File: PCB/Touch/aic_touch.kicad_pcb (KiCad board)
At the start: 2 copper layers, 50 x 50 mm, 14 parts, among them J1 Antenna, J2 PN5180, J3 PN532, J4 Display, U1 Pico

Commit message: Fix PCB issue and change to 4020 RGB
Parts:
- D1, D2, D3, D4, D5, D6: footprint aic_pico:WS2812B-1204 -> aic_pico:WS2812B-4020
- moved D1 36.8 mm to (153.7, 122.3)
- moved D2 36.8 mm to (153.7, 104.5)
- moved D5 36.8 mm to (116.9, 104.5)
- moved D6 36.8 mm to (116.9, 122.3)
- moved R1 36.2 mm to (153.1, 126.4)
- moved D3 16.5 mm to (143.6, 95.0), turned to 0 degrees
- moved D4 16.5 mm to (127.1, 95.0), turned to 0 degrees
- moved R2 6.41 mm to (137.1, 102.0), turned to 0 degrees
- moved R3 5.38 mm to (133.5, 102.0)
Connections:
- U1 pad 10: /TP_SCL -> /RST
- U1 pad 11: /TP_RST -> /D/C
- U1 pad 12: /TP_INT -> /CS
- U1 pad 14: unconnected-(U1-GPIO10-Pad14) -> /SCK
- U1 pad 15: unconnected-(U1-GPIO11-Pad15) -> /SDA
- U1 pad 2: /D/C -> unconnected-(U1-GPIO1-Pad2)
- U1 pad 4: /SCK -> /TP_SDA
- U1 pad 5: /SDA -> /TP_SCL
- U1 pad 6: /RST -> /TP_INT
- U1 pad 7: /CS -> /TP_RST
- U1 pad 9: /TP_SDA -> unconnected-(U1-GPIO6-Pad9)
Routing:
- net /RGB: track 31.1 -> 13.4 mm
- net /D/C: track 27.2 -> 12.5 mm
- net +3V3: track 92.4 -> 105.3 mm
- net /SCK: track 23.1 -> 15.9 mm
- net GND: track 204.4 -> 198.1 mm
- net /RST: track 20.5 -> 14.4 mm
- net /TP_SDA: track 18.9 -> 24.8 mm
- net /LEDK: track 32.6 -> 27.3 mm
- net /TP_INT: track 16.3 -> 21.3 mm
- net /TP_RST: track 14.0 -> 19.0 mm
- net Net-(D4-Out): track 16.9 -> 13.3 mm
- net /SDA: track 22.3 -> 18.8 mm
- net +5V: track 153.2 -> 150.3 mm
- net /TP_SCL: track 20.4 -> 22.9 mm
- net Net-(D1-In): track 4.39 -> 1.96 mm
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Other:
- board text added: "AIC Touch v1.1"
- board text removed: "AIC Touch v1.0"

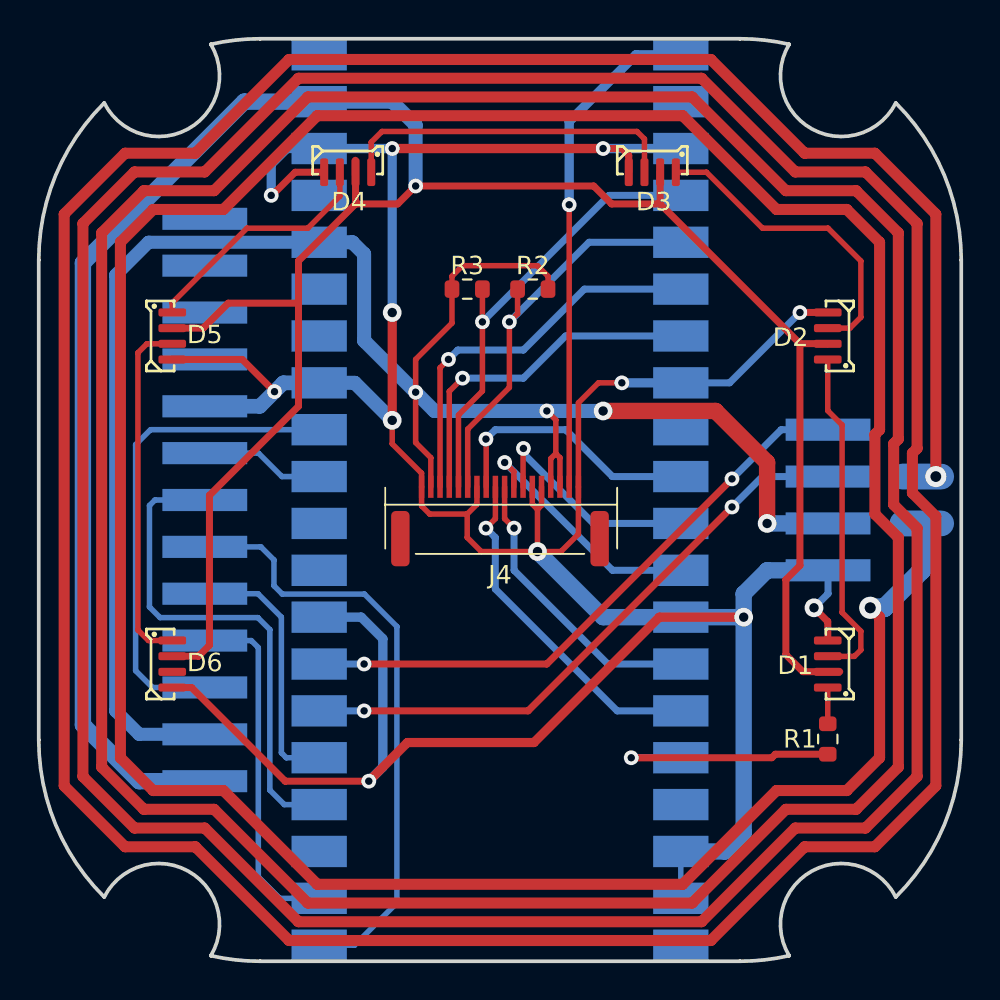
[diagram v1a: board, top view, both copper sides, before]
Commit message: Power filtering for PN5180 on AIC touch
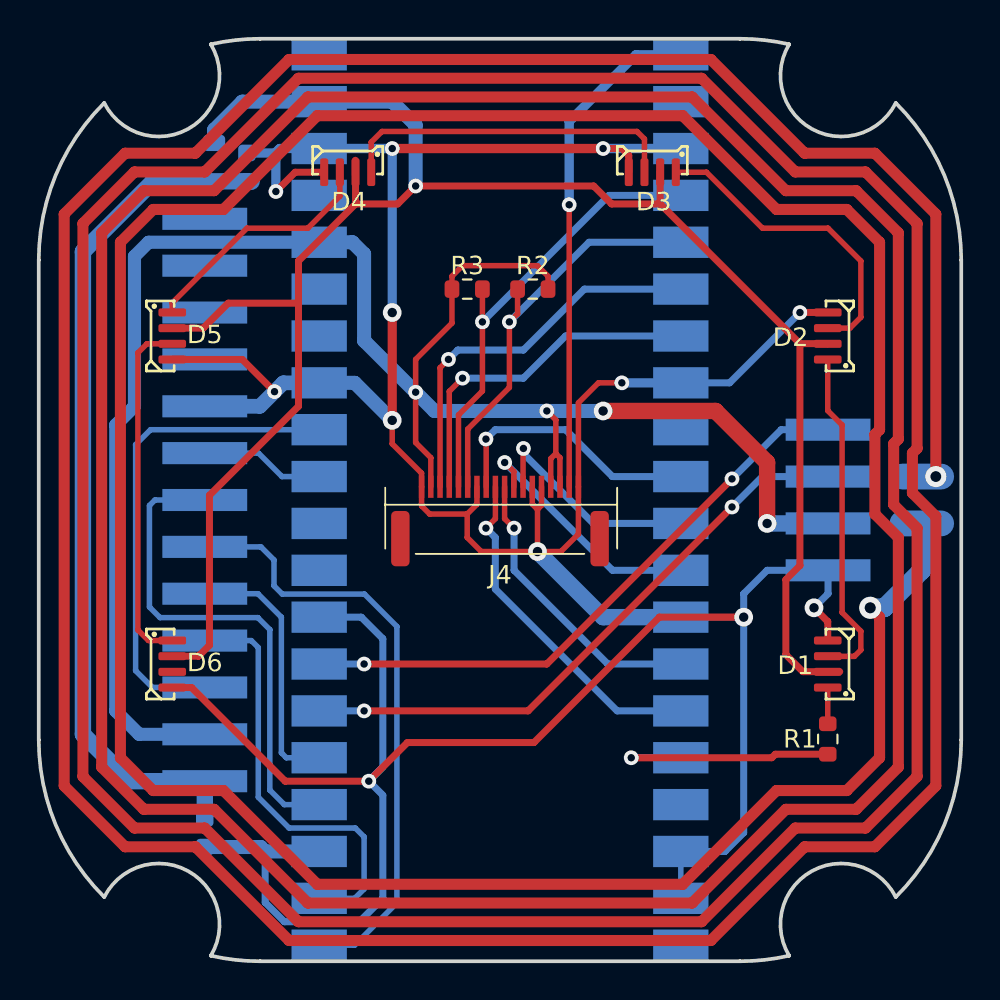
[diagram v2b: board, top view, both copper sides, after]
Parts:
- added C1: 0.1uF, Capacitor_SMD:C_0603_1608Metric, B.Cu at (121.6, 95.4)
- added C2: 10uF, Capacitor_SMD:C_0603_1608Metric, B.Cu at (119.3, 131.4)
- added L1: 100nH, Inductor_SMD:L_0805_2012Metric, B.Cu at (119.8, 95.1)
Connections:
- J2 pad 1: +5V -> Net-(J2-5V)
- U1 pad 23: unconnected-(U1-GND-Pad23) -> GND
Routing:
- net Net-(J2-5V): track 0.00 -> 46.6 mm
- net +5V: track 150.3 -> 107.2 mm
- net GND: track 198.1 -> 222.6 mm
- net Net-(J2-NSS): track 19.3 -> 23.3 mm
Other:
- board text added: "AIC Touch v1.2"
- board text removed: "AIC Touch v1.1"

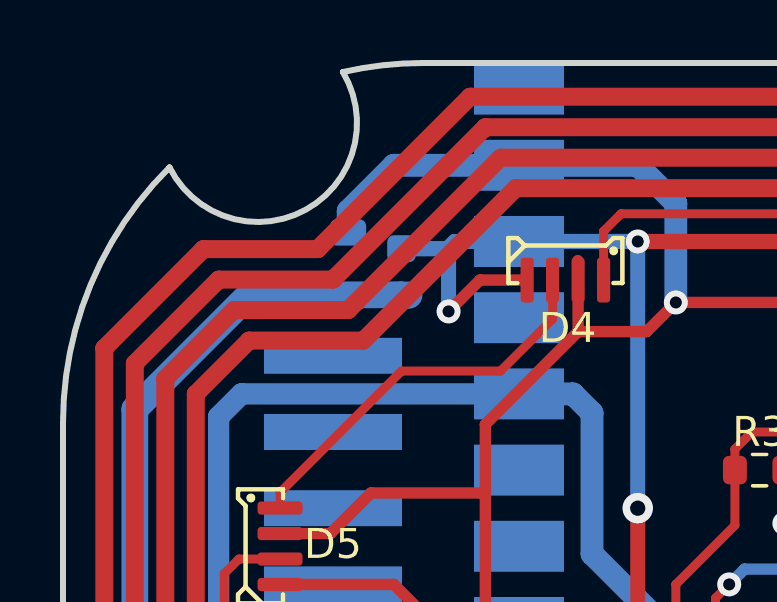
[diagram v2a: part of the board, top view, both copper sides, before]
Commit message: L1 to 1206 and power from VBUS
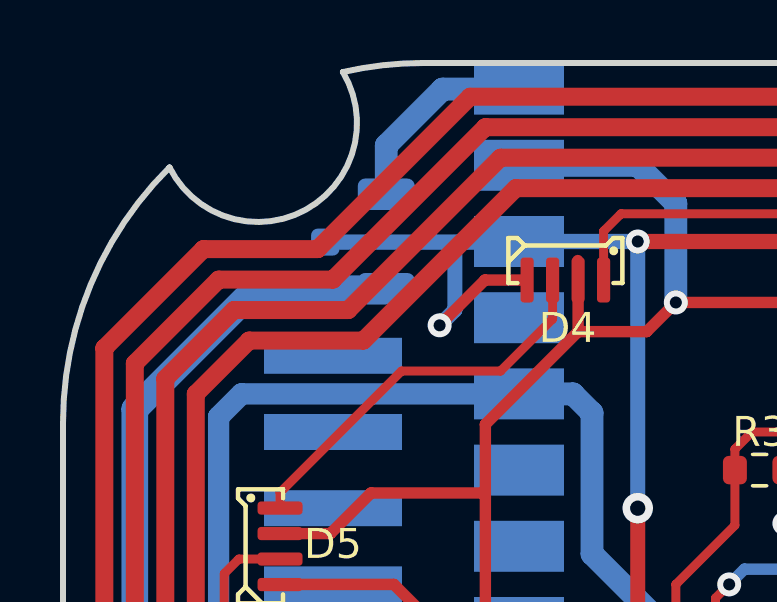
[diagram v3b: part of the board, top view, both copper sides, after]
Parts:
- L1: footprint Inductor_SMD:L_0805_2012Metric -> Inductor_SMD:L_1206_3216Metric
- moved C1 2.55 mm to (119.1, 95.1)
- moved L1 1.48 mm to (121.1, 94.3)
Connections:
- L1 pad 1: +5V -> Net-(U1-VBUS)
- U1 pad 40: unconnected-(U1-VBUS-Pad40) -> Net-(U1-VBUS)
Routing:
- net +5V: track 107.2 -> 100.2 mm
- net Net-(U1-VBUS): track 0.00 -> 6.83 mm
- net GND: track 222.6 -> 226.1 mm
- net Net-(J2-5V): track 46.6 -> 45.9 mm
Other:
- board text added: "AIC Touch v1.21"
- board text removed: "AIC Touch v1.2"

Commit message: Hybrid AIC Key PCB and AIC touch RGB back to 1204
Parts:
- removed L1: 100nH, Inductor_SMD:L_1206_3216Metric
- added C3: 0.1uF, Capacitor_SMD:C_0603_1608Metric, F.Cu at (140.9, 110.1)
- C2: value 10uF -> 0.1uF; moved to F.Cu
- D1, D2, D3, D4, D5, D6: footprint aic_pico:WS2812B-4020 -> aic_pico:WS2812B-1204
- moved R1 35.8 mm to (117.3, 126.6), turned to 0 degrees
- moved D1 35.4 mm to (118.3, 122.4)
- moved D2 35.4 mm to (118.3, 104.4)
- moved D5 35.4 mm to (152.3, 104.4)
- moved D6 35.4 mm to (152.3, 122.4)
- moved C2 24.0 mm to (130.2, 110.1), turned to 180 degrees
- moved D3 17.3 mm to (126.3, 96.4), turned to 180 degrees
- moved D4 17.3 mm to (144.3, 96.4), turned to 180 degrees
- moved C1 2.03 mm to (121.1, 95.1), turned to -90 degrees
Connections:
- C1 pad 1: Net-(J2-5V) -> +5V
- C2 pad 1: Net-(J2-5V) -> +3V3
- J2 pad 1: Net-(J2-5V) -> +5V
- U1 pad 40: Net-(U1-VBUS) -> unconnected-(U1-VBUS-Pad40)
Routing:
- net +5V: track 100.2 -> 146.4 mm
- net Net-(J2-5V): track 45.9 -> 0.00 mm
- net GND: track 226.1 -> 202.7 mm
- net /RGB: track 13.4 -> 29.2 mm
- net Net-(U1-VBUS): track 6.83 -> 0.00 mm
- net Net-(D2-Out): track 17.1 -> 11.0 mm
- net Net-(J2-NSS): track 23.3 -> 19.3 mm
- net Net-(D1-In): track 1.96 -> 5.03 mm
- net Net-(D4-Out): track 13.3 -> 15.2 mm
- net Net-(D5-Out): track 19.2 -> 18.2 mm
- net Net-(D3-Out): track 18.7 -> 19.5 mm
- net +3V3: track 105.3 -> 106.2 mm
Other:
- board text added: "AIC Touch v1.3"
- board text added: "PN5180"
- board text added: "PN532"
- board text removed: "AIC Touch v1.21"

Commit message: Touch PCB v1.4 (may improve RF)
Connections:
- J2 pad 9: GND -> /5180_GND
- J3 pad 1: GND -> /532_GND
- U1 pad 13: GND -> /532_GND
- U1 pad 18: GND -> Net-(U1-GPIO14)
- U1 pad 19: GND -> Net-(U1-GPIO14)
- U1 pad 23: GND -> unconnected-(U1-GND-Pad23)
- U1 pad 28: GND -> unconnected-(U1-GND-Pad28)
- U1 pad 3: GND -> unconnected-(U1-GND-Pad3)
- U1 pad 33: GND -> /5180_GND
- U1 pad 8: GND -> unconnected-(U1-GND-Pad8)
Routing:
- net GND: track 202.7 -> 149.4 mm, vias 12 -> 7
- net /532_GND: track 0.00 -> 9.03 mm
- net /5180_GND: track 0.00 -> 6.73 mm
- net Net-(U1-GPIO14): track 0.00 -> 2.54 mm
- net +5V: track 146.4 -> 144.0 mm
- net /RGB: track 29.2 -> 27.3 mm
- net Net-(J2-MISO): track 33.2 -> 32.4 mm
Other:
- board text added: "AIC Touch v1.4"
- board text removed: "AIC Touch v1.3"

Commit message: Offload PN532 antenna for better signal
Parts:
- added J5: Antenna, aic_pico:ANT_3P, B.Cu at (111.7, 113.4)
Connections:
- J1 pad 1: /ANT -> /ANT_1
- J1 pad 2: /ANT -> /ANT_2
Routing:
- net /ANT: track 640.9 -> 0.00 mm, vias 2 -> 0
- net /ANT_1: track 0.00 -> 556.6 mm, vias 0 -> 3
- net /ANT_2: track 0.00 -> 83.7 mm, vias 0 -> 2
- net +3V3: track 105.8 -> 89.0 mm, vias 4 -> 6
- net Net-(J2-RST): track 26.7 -> 16.9 mm, vias 0 -> 2
- net +5V: track 144.0 -> 140.2 mm
- net /RGB: track 27.3 -> 28.1 mm
- net Net-(J2-SCK): track 27.4 -> 27.8 mm, vias 0 -> 2
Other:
- board text added: "AIC Touch v1.5"
- board text added: "PN5180 ANT"
- board text added: "PN532 ANT"
- board text removed: "AIC Touch v1.4"

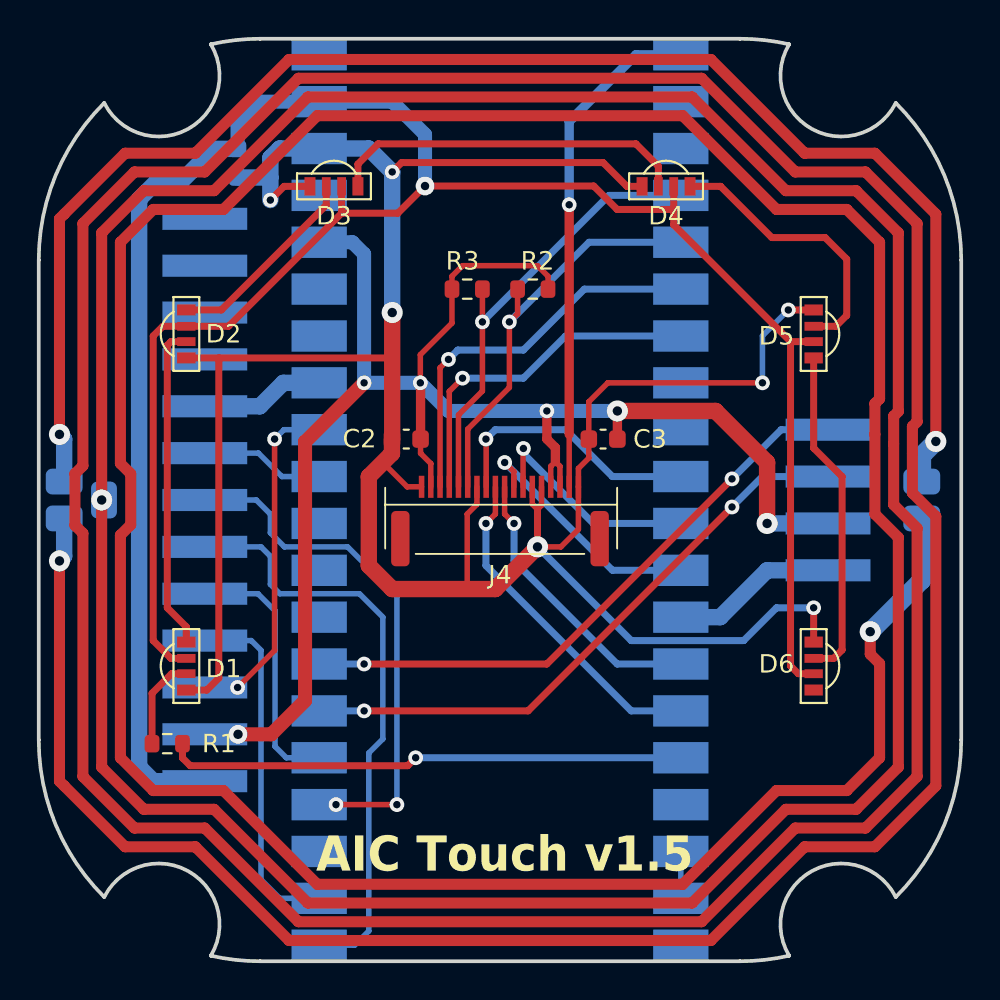
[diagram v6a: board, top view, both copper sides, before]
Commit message: Touch PCB v1.51, optimize footprints
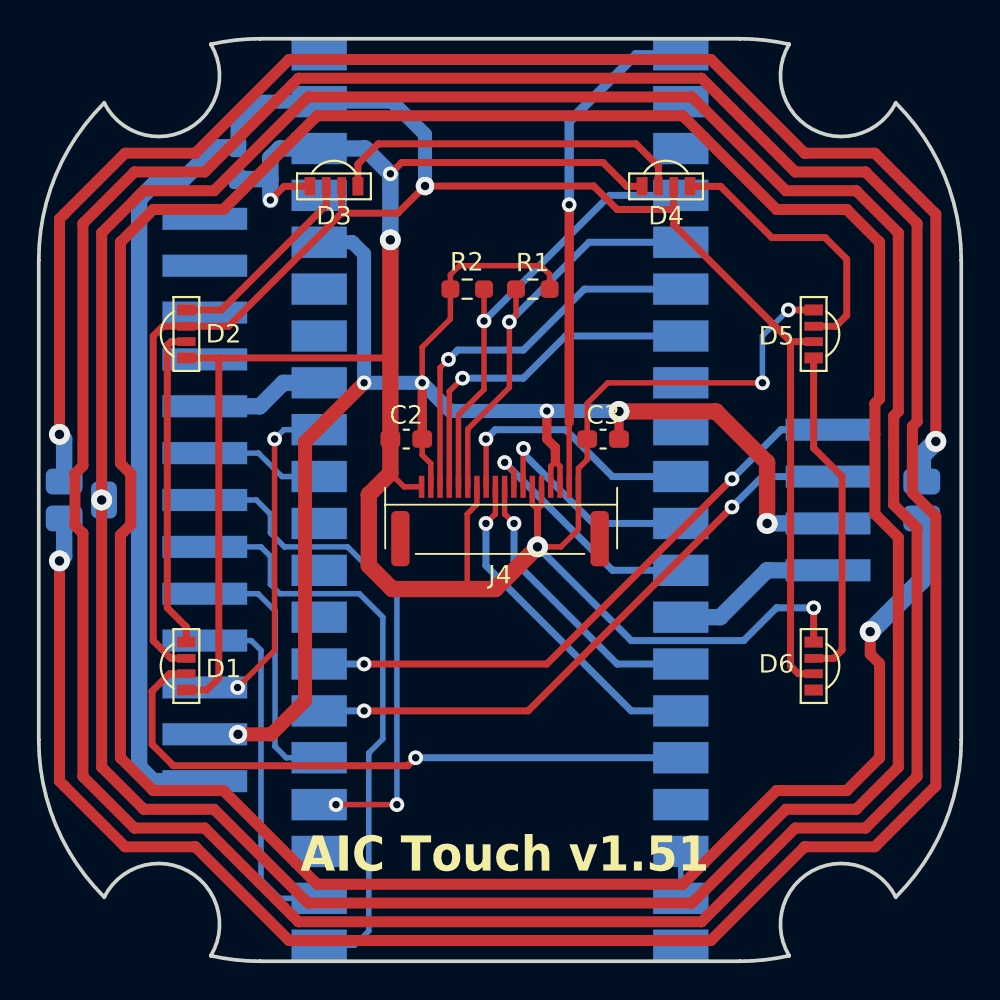
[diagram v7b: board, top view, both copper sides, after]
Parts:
- removed the R1 at (117.3, 126.6)
- C1, C2, C3: footprint Capacitor_SMD:C_0603_1608Metric -> Capacitor_SMD:C_0603_1608Metric_Pad1.08x0.95mm_HandSolder
- R1: renamed from R2; footprint Resistor_SMD:R_0603_1608Metric -> Resistor_SMD:R_0603_1608Metric_Pad0.98x0.95mm_HandSolder
- R2: renamed from R3; footprint Resistor_SMD:R_0603_1608Metric -> Resistor_SMD:R_0603_1608Metric_Pad0.98x0.95mm_HandSolder
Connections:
- D1 pad I: Net-(D1-In) -> /RGB
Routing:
- net /RGB: track 28.1 -> 34.5 mm
- net Net-(D1-In): track 5.03 -> 0.00 mm
- net GND: track 149.4 -> 148.6 mm
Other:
- board text added: "AIC Touch v1.51"
- board text removed: "AIC Touch v1.5"
